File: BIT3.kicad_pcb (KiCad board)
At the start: 2 copper layers, 121.3 x 109.4 mm, 45 parts, among them J1 Conn_02x04_Odd_Even, J2 Conn_01x02_Pin, Q1 2SC1815, SW1 SW_SPDT, SW2 SW_Push, SW3 SW_Push, U2 SG-107F, U3 SG-107F, U4 SG-107F, U5 SG-107F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

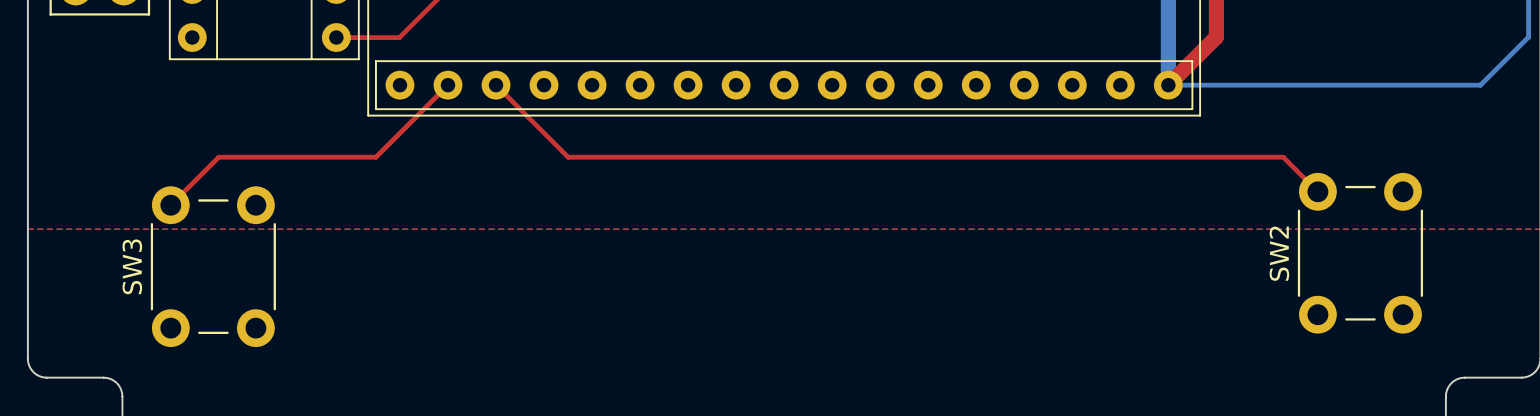
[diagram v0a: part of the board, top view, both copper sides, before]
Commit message: Update PCB Design
- remove `SW2` and `SW3` silkscreen
- add silkscreen print
  - `SW2` as `MODE`, `SW3` as `BACK`
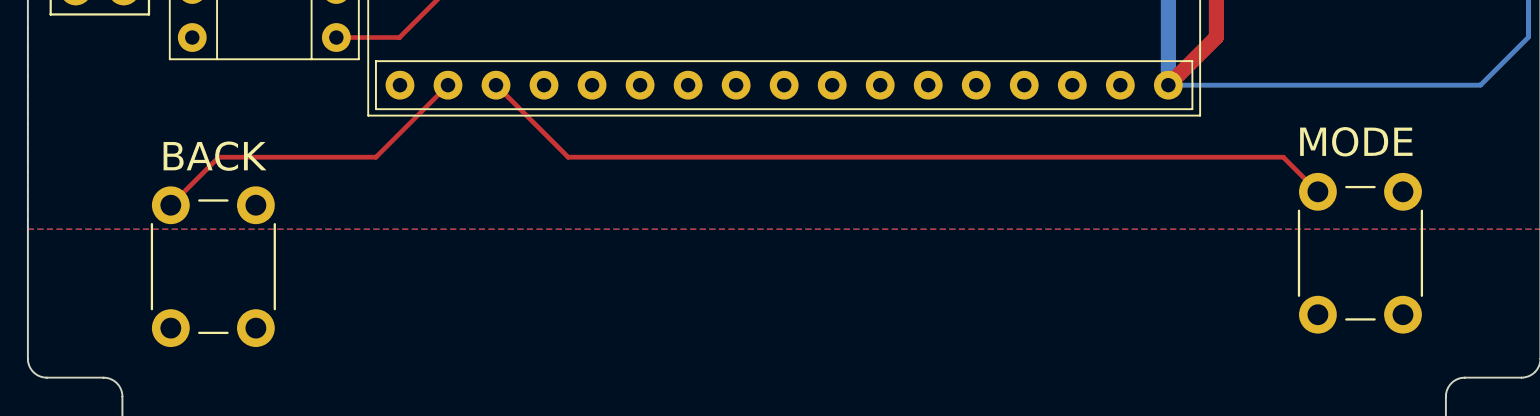
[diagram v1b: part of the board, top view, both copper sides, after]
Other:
- board text added: "BACK"
- board text added: "MODE"
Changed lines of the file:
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@@
       (sketchpadsonfab false)
       (subtractmaskfromsilk false)
-      (outputformat 1)
+      (outputformat 5)
       (mirror false)
       (drillshape 0)
@@
     (property "ki_keywords" "switch normally-open pushbutton push-button")
     (attr through_hole)
-    (fp_text reference "SW2" (at 3.25 -2 90) (layer "F.SilkS")
+    (fp_text reference "SW2" (at 3.25 -2 90) (layer "F.SilkS") hide
         (effects (font (size 1 1) (thickness 0.15)))
     )
@@
     (property "ki_keywords" "switch normally-open pushbutton push-button")
     (attr through_hole)
-    (fp_text reference "SW3" (at 3.25 -2 90) (layer "F.SilkS")
+    (fp_text reference "SW3" (at 3.25 -2 90) (layer "F.SilkS") hide
         (effects (font (size 1 1) (thickness 0.15)))
     )
@@
     )
   )
+  (gr_text "BACK" (at 122.174 116.84) (layer "F.SilkS")
+    (effects (font (size 1.5 1.5) (thickness 0.2)))
+  )
   (gr_text "Bat" (at 116.078 69.85) (layer "F.SilkS")
     (effects (font (size 1 1) (thickness 0.15)))
   )
+  (gr_text "MODE" (at 182.626 116.078) (layer "F.SilkS")
+    (effects (font (size 1.5 1.5) (thickness 0.2)))
+  )
   (gr_text "GND" (at 117.348 70.485) (layer "F.SilkS")

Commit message: Update PCB Design
add GND vias
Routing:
- net GND: vias 0 -> 3
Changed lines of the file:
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@@
   )
   (segment (start 137.265 46.895) (end 137.265 47.53) (width 0.25) (layer "F.Cu") (net 1))
+  (via (at 190.5 78.486) (size 0.8) (drill 0.4) (layers "F.Cu" "B.Cu") (free) (net 1))
+  (via (at 192.786 77.724) (size 0.8) (drill 0.4) (layers "F.Cu" "B.Cu") (free) (net 1))
+  (via (at 190.5 79.502) (size 0.8) (drill 0.4) (layers "F.Cu" "B.Cu") (free) (net 1))
   (segment (start 221.615 77.354) (end 222.49 76.479) (width 0.25) (layer "B.Cu") (net 1))
   (segment (start 228.366 76.479) (end 228.595 76.708) (width 0.25) (layer "B.Cu") (net 1))

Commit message: Update PCB Design
fix Power Supply
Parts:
- moved G*** 0.74 mm to (152.4, 63.8)
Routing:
- net +BATT: track 23.8 -> 33.7 mm
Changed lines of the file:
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@@
   )
   (footprint "LOGO" (layer "F.Cu")
-    (at 153.035 64.135)
+    (at 152.4 63.754)
     (attr board_only exclude_from_pos_files exclude_from_bom)
-    (fp_text reference "G***" (at 0 0) (layer "F.SilkS")
+    (fp_text reference "G***" (at 0 0) (layer "F.SilkS") hide
         (effects (font (size 1.5 1.5) (thickness 0.3)))
     )
@@
   (segment (start 134.62 45.72) (end 137.89 45.72) (width 0.25) (layer "F.Cu") (net 34))
   (segment (start 137.89 45.72) (end 139.065 46.895) (width 0.25) (layer "F.Cu") (net 34))
+  (segment (start 121.095 97.81) (end 121.095 91.379) (width 0.8) (layer "F.Cu") (net 37))
+  (segment (start 119.414 89.698) (end 118.364 89.698) (width 0.8) (layer "F.Cu") (net 37))
+  (segment (start 121.095 91.379) (end 119.414 89.698) (width 0.8) (layer "F.Cu") (net 37))
   (segment (start 127 82.55) (end 127 85.725) (width 0.25) (layer "B.Cu") (net 37))
   (segment (start 123.027 89.698) (end 118.364 89.698) (width 0.25) (layer "B.Cu") (net 37))

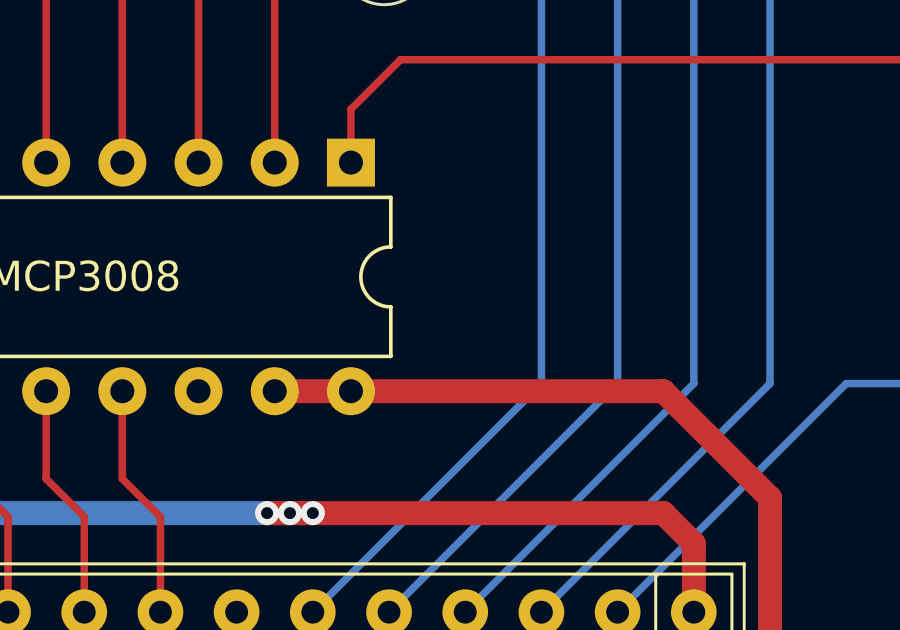
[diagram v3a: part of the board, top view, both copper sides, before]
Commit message: 基板更新
MCP3008 にパスコンを追加
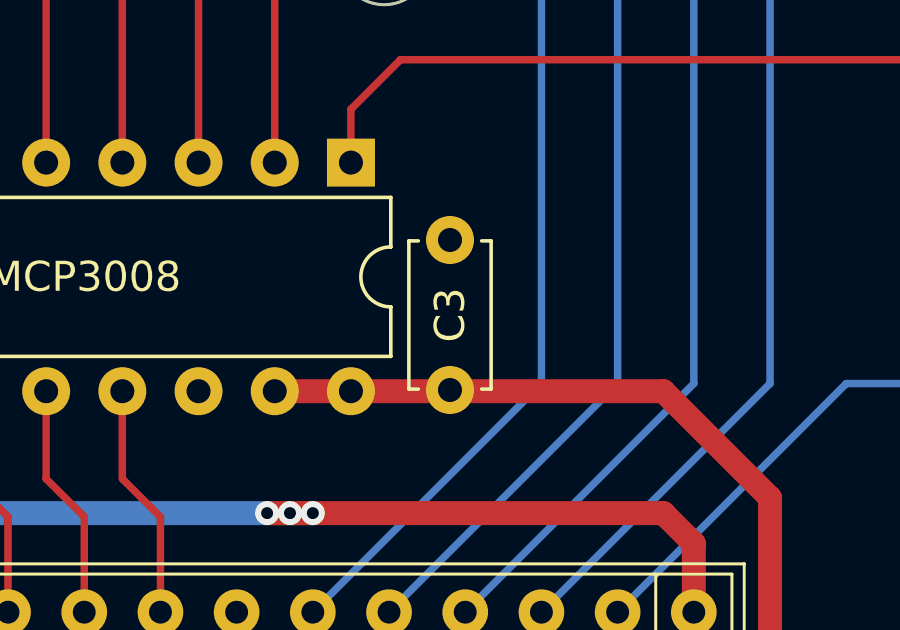
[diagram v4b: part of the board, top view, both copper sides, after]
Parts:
- added C3: C, Capacitor_THT:C_Disc_D4.7mm_W2.5mm_P5.00mm, F.Cu at (164.6, 87.8)
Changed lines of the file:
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@@
       (sketchpadsonfab false)
       (subtractmaskfromsilk false)
-      (outputformat 5)
+      (outputformat 1)
       (mirror false)
       (drillshape 0)
@@
       (offset (xyz 0 0 0))
       (scale (xyz 1 1 1))
+      (rotate (xyz 0 0 0))
+    )
+  )
+  (footprint "Capacitor_THT:C_Disc_D4.7mm_W2.5mm_P5.00mm" (layer "F.Cu")
+    (at 164.592 87.844 90)
+    (descr "C, Disc series, Radial, pin pitch=5.00mm, , diameter*width=4.7*2.5mm^2, Capacitor, http://www.vishay.com/docs/45233/krseries.pdf")
+    (tags "C Disc series Radial pin pitch 5.00mm  diameter 4.7mm width 2.5mm Capacitor")
+    (property "Sheetfile" "BIT3.kicad_sch")
+    (property "Sheetname" "")
+    (property "ki_description" "Unpolarized capacitor")
+    (property "ki_keywords" "cap capacitor")
+    (attr through_hole)
+    (fp_text reference "C3" (at 2.5 0 90) (layer "F.SilkS")
+        (effects (font (size 1 1) (thickness 0.15)))
+    )
+    (fp_text value "C" (at 2.5 2.5 90) (layer "F.Fab")
+        (effects (font (size 1 1) (thickness 0.15)))
+    )
+    (fp_text user "${REFERENCE}" (at 2.5 0 90) (layer "F.Fab")
+        (effects (font (size 0.94 0.94) (thickness 0.141)))
+    )
+    (fp_line (start 0.03 -1.37) (end 0.03 -1.055)
+      (stroke (width 0.12) (type solid)) (layer "F.SilkS"))
+    (fp_line (start 0.03 -1.37) (end 4.97 -1.37)
+      (stroke (width 0.12) (type solid)) (layer "F.SilkS"))
+    (fp_line (start 0.03 1.055) (end 0.03 1.37)
+      (stroke (width 0.12) (type solid)) (layer "F.SilkS"))
+    (fp_line (start 0.03 1.37) (end 4.97 1.37)
+      (stroke (width 0.12) (type solid)) (layer "F.SilkS"))
+    (fp_line (start 4.97 -1.37) (end 4.97 -1.055)
+      (stroke (width 0.12) (type solid)) (layer "F.SilkS"))
+    (fp_line (start 4.97 1.055) (end 4.97 1.37)
+      (stroke (width 0.12) (type solid)) (layer "F.SilkS"))
+    (fp_line (start -1.05 -1.5) (end -1.05 1.5)
+      (stroke (width 0.05) (type solid)) (layer "F.CrtYd"))
+    (fp_line (start -1.05 1.5) (end 6.05 1.5)
+      (stroke (width 0.05) (type solid)) (layer "F.CrtYd"))
+    (fp_line (start 6.05 -1.5) (end -1.05 -1.5)
+      (stroke (width 0.05) (type solid)) (layer "F.CrtYd"))
+    (fp_line (start 6.05 1.5) (end 6.05 -1.5)
+      (stroke (width 0.05) (type solid)) (layer "F.CrtYd"))
+    (fp_line (start 0.15 -1.25) (end 0.15 1.25)
+      (stroke (width 0.1) (type solid)) (layer "F.Fab"))
+    (fp_line (start 0.15 1.25) (end 4.85 1.25)
+      (stroke (width 0.1) (type solid)) (layer "F.Fab"))
+    (fp_line (start 4.85 -1.25) (end 0.15 -1.25)
+      (stroke (width 0.1) (type solid)) (layer "F.Fab"))
+    (fp_line (start 4.85 1.25) (end 4.85 -1.25)
+      (stroke (width 0.1) (type solid)) (layer "F.Fab"))
+    (pad "1" thru_hole circle (at 0 0 90) (size 1.6 1.6) (drill 0.8) (layers "*.Cu" "*.Mask")
+      (net 2 "+3V3") (pintype "passive"))
+    (pad "2" thru_hole circle (at 5 0 90) (size 1.6 1.6) (drill 0.8) (layers "*.Cu" "*.Mask")
+      (net 1 "GND") (pintype "passive"))
+    (model "${KICAD6_3DMODEL_DIR}/Capacitor_THT.3dshapes/C_Disc_D4.7mm_W2.5mm_P5.00mm.wrl"
+      (offset (xyz 0 0 0))
+      (scale (xyz 1 1 1))

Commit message: Update PCB Design
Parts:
- moved G*** 1.25 mm to (152.4, 65.0)
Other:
- outline, holes or cut-outs redrawn
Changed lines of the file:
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@@
   )
   (footprint "LOGO" (layer "F.Cu")
-    (at 152.4 63.754)
+    (at 152.4 65)
     (attr board_only exclude_from_pos_files exclude_from_bom)
     (fp_text reference "G***" (at 0 0) (layer "F.SilkS") hide
@@
   (gr_arc (start 187.4 147.5) (mid 187.107107 148.207107) (end 186.4 148.5)
     (stroke (width 0.1) (type default)) (layer "Edge.Cuts"))
-  (gr_circle (center 142.4 53.5) (end 143.9 53.5)
+  (gr_circle (center 142.4 54.746) (end 143.9 54.746)
     (stroke (width 0.1) (type default)) (fill none) (layer "Edge.Cuts"))
   (gr_arc (start 187.4 129.5) (mid 187.692893 128.792893) (end 188.4 128.5)
@@
   (gr_line (start 233.68 75) (end 233.68 78.5)
     (stroke (width 0.1) (type default)) (layer "Edge.Cuts"))
-  (gr_circle (center 162.4 53.5) (end 160.9 53.5)
+  (gr_circle (center 162.4 54.746) (end 160.9 54.746)
     (stroke (width 0.1) (type default)) (fill none) (layer "Edge.Cuts"))
   (gr_line (start 192.4 127.5) (end 192.4 81.5)
@@
   (gr_arc (start 112.4 48.5) (mid 152.4 39.057281) (end 192.4 48.5)
     (stroke (width 0.1) (type default)) (layer "Edge.Cuts"))
-  (gr_circle (center 162.4 73.5) (end 160.9 73.5)
+  (gr_circle (center 162.4 74.746) (end 160.9 74.746)
     (stroke (width 0.1) (type default)) (fill none) (layer "Edge.Cuts"))
   (gr_line (start 192.4 48.5) (end 192.4 72)
@@
   (gr_line (start 194.4 74) (end 232.68 74)
     (stroke (width 0.1) (type default)) (layer "Edge.Cuts"))
-  (gr_circle (center 142.4 73.5) (end 143.9 73.5)
+  (gr_circle (center 142.4 74.746) (end 143.9 74.746)
     (stroke (width 0.1) (type default)) (fill none) (layer "Edge.Cuts"))
   (gr_line (start 187.4 147.5) (end 187.4 129.5)

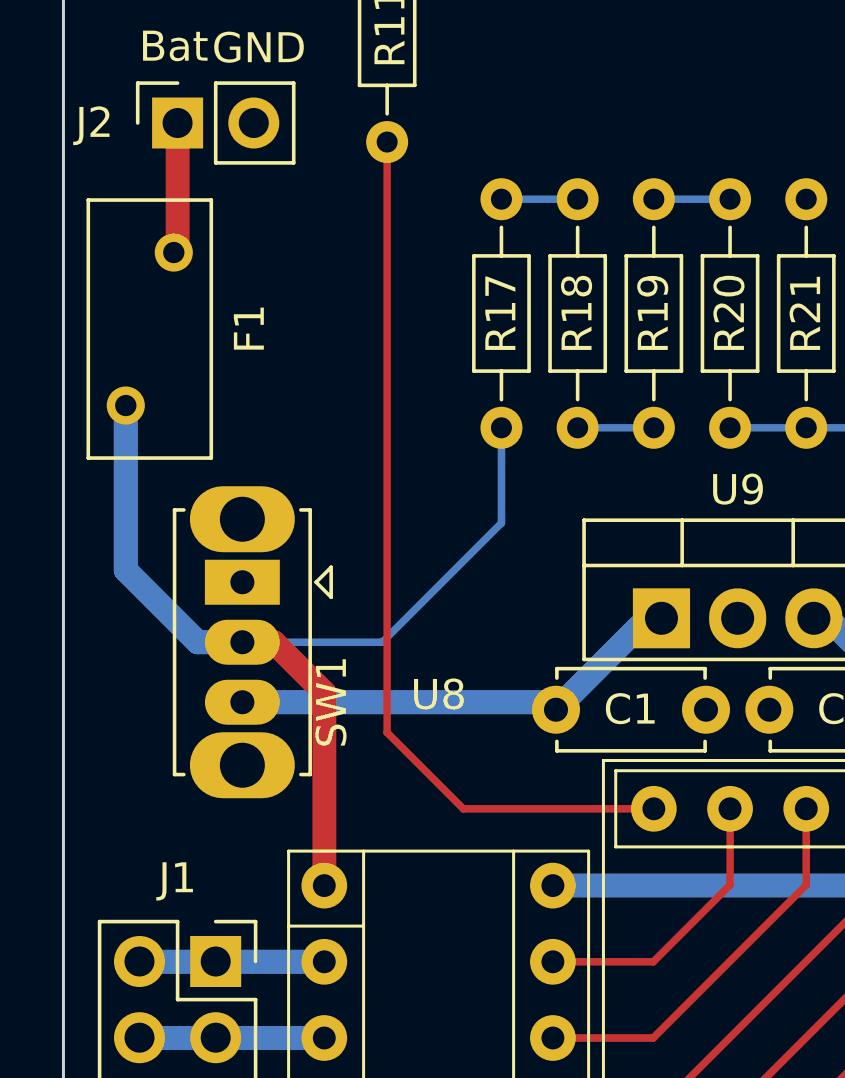
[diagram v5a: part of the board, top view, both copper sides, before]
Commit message: 逆説防止 D を追加, バッテリ電圧監視 ADC の配置を変更
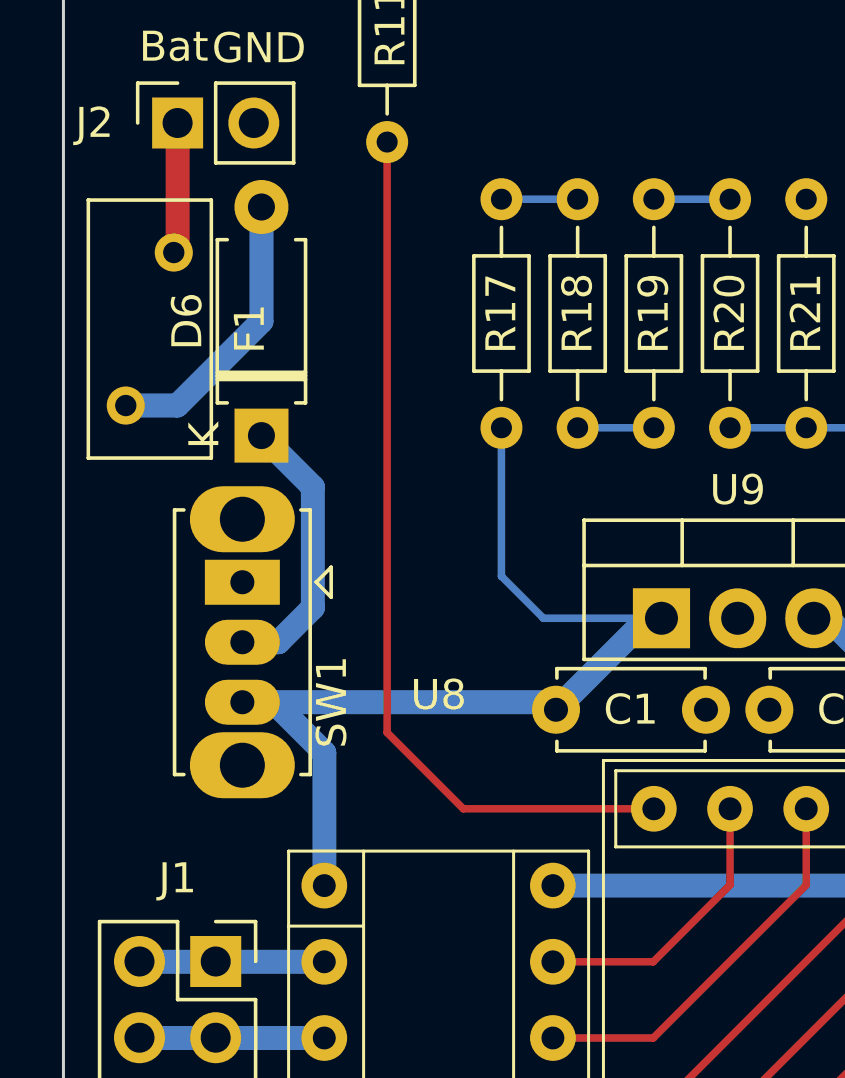
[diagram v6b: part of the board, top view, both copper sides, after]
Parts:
- added D6: D, Diode_THT:D_A-405_P7.62mm_Horizontal, F.Cu at (119.0, 82.8)
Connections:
- C1 pad 1: Net-(SW1-C) -> /V_Battery
- R17 pad 1: +BATT -> /V_Battery
- SW1 pad 2: +BATT -> Net-(D6-K)
- SW1 pad 3: Net-(SW1-C) -> /V_Battery
- U8 pad 1: +BATT -> /V_Battery
- U9 pad 1: Net-(SW1-C) -> /V_Battery
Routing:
- net /V_Battery: track 0.00 -> 34.1 mm
- net +BATT: track 33.7 -> 9.50 mm
- net Net-(SW1-C): track 15.3 -> 0.00 mm
- net Net-(D6-K): track 0.00 -> 9.27 mm

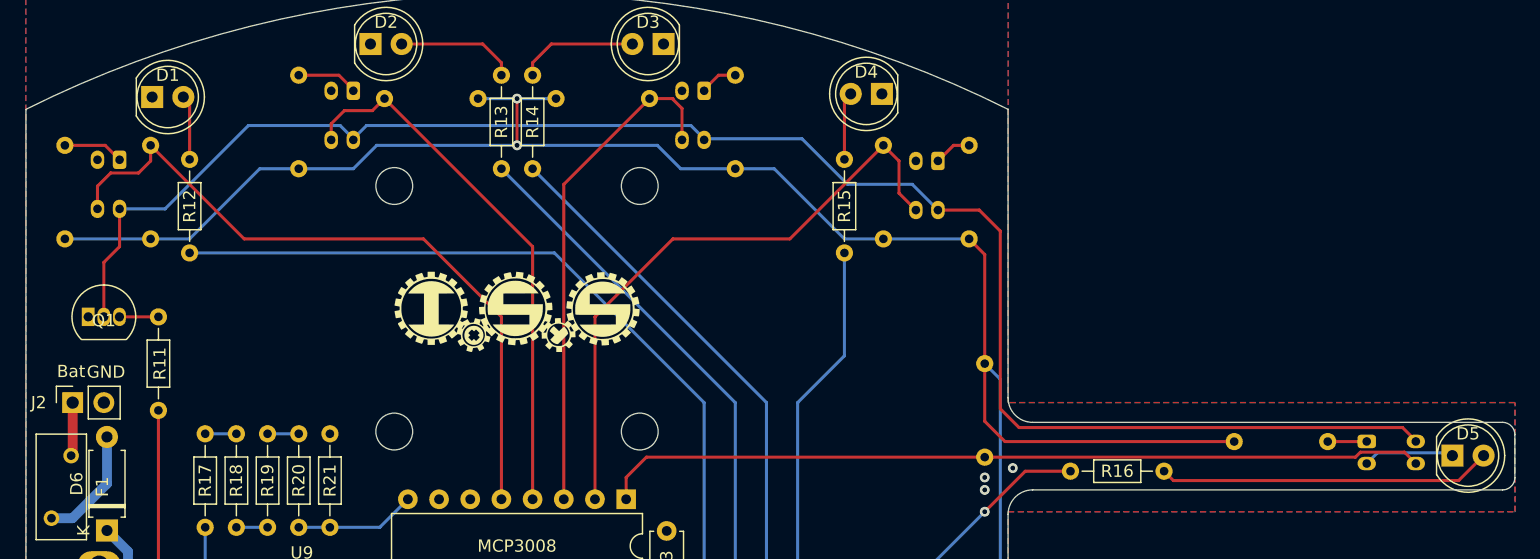
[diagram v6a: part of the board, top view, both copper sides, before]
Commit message: フォトセンサを変更
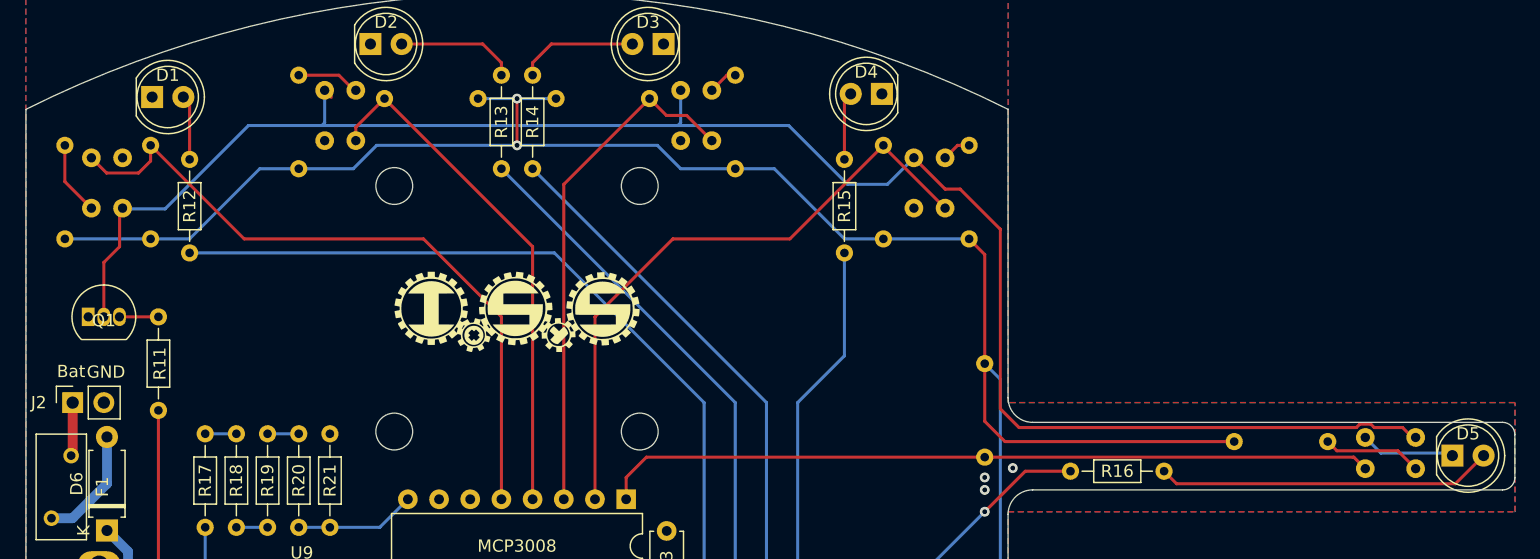
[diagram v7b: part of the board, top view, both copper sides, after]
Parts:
- U2, U3, U4, U5, U6: value SG-107F -> FODM217A; footprint OptoDevice:Kodenshi_SG105F -> AE-Parts:LBR-127HLD
- moved U3 29.7 mm to (138.0, 49.0)
- moved U4 28.0 mm to (167.0, 49.0)
- moved U6 2.15 mm to (223.6, 76.5), turned to 90 degrees
- moved U2 2.15 mm to (119.0, 54.5), turned to 0 degrees
- moved U5 1.92 mm to (186.0, 54.5)
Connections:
- R2 pad 2: Net-(U3-A) -> Net-(R2-Pad2)
- R3 pad 2: Net-(U4-A) -> Net-(R3-Pad2)
- U2 pad 3: /sensor_L -> GND
- U2 pad 4: GND -> /sensor_L
- U3 pad 1: Net-(U3-A) -> Net-(R3-Pad2)
- U3 pad 3: /sensor_CR -> GND
- U3 pad 4: GND -> /sensor_CL
- U4 pad 1: Net-(U4-A) -> Net-(R2-Pad2)
- U4 pad 3: /sensor_CL -> GND
- U4 pad 4: GND -> /sensor_CR
- U5 pad 3: /sensor_R -> GND
- U5 pad 4: GND -> /sensor_R
- U6 pad 3: /sensor_Goal -> GND
- U6 pad 4: GND -> /sensor_Goal
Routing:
- net /FET_D: track 137.8 -> 145.7 mm
- net Net-(U4-A): track 4.93 -> 0.00 mm
- net Net-(R3-Pad2): track 0.00 -> 4.93 mm
- net Net-(R5-Pad2): track 3.18 -> 8.07 mm
- net /sensor_Goal: track 67.3 -> 63.1 mm
- net Net-(U3-A): track 3.03 -> 0.00 mm
- net Net-(R2-Pad2): track 0.00 -> 2.42 mm
- net /sensor_CL: track 44.1 -> 42.0 mm
- net /sensor_L: track 57.5 -> 56.2 mm
- net Net-(R1-Pad2): track 4.94 -> 6.01 mm
- net /sensor_CR: track 41.1 -> 42.0 mm
- net /sensor_R: track 50.5 -> 51.3 mm
- net Net-(R4-Pad2): track 3.07 -> 2.38 mm
